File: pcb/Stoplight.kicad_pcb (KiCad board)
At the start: 2 copper layers, 39.7 x 33.1 mm, 13 parts, among them IC1 ATtiny85-20M, IC2 AP7375-33SA-7

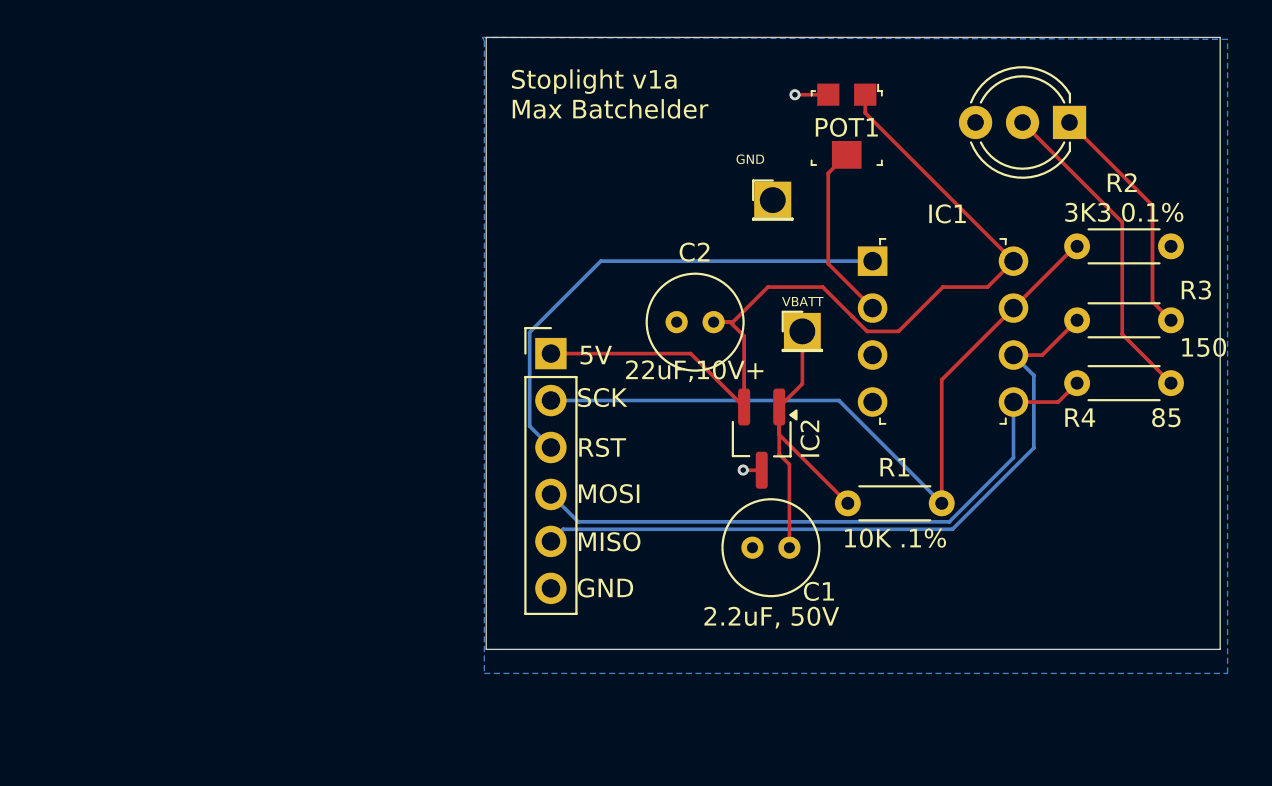
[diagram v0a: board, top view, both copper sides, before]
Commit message: redesigning pcb to be smaller & use tag-connect
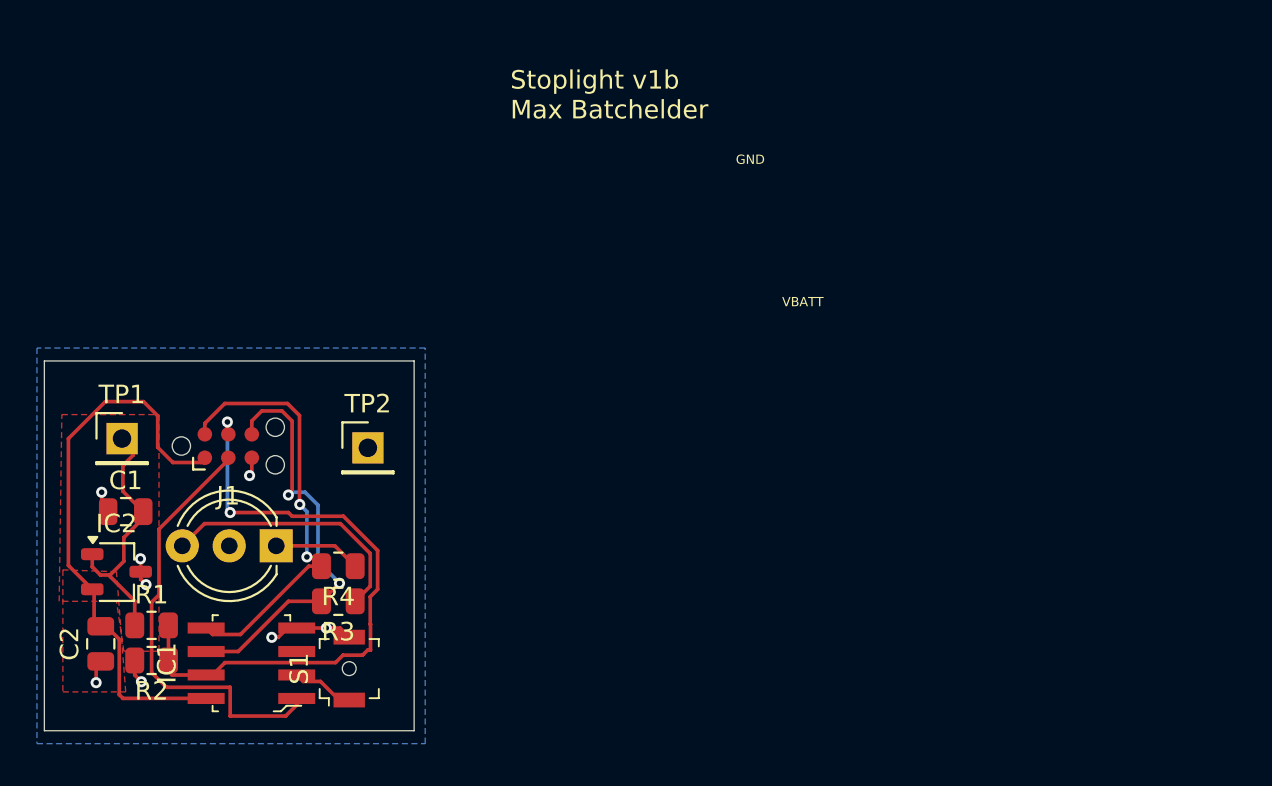
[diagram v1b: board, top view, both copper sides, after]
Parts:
- removed POT1: TC33X-2-103E, digikey-footprints:Trimpot_3.8mmx3.6mm_TC33X-2-103E
- removed REF**: PinHeader_1x06_P2.54mm_Vertical, Connector_PinHeader_2.54mm:PinHeader_1x06_P2.54mm_Vertical
- added J1: Conn_ARM_SWD_TagConnect_TC2030-NL, Connector:Tag-Connect_TC2030-IDC-NL_2x03_P1.27mm_Vertical, F.Cu at (110.0, 104.6)
- added S1: B3U-1000P, digikey-footprints:Switch_Tactile_SMD_B3U-1000P, F.Cu at (116.5, 116.6)
- C1, C2: footprint Capacitor_THT:C_Radial_D5.0mm_H5.0mm_P2.00mm -> Capacitor_SMD:C_0805_2012Metric
- IC1: footprint digikey-footprints:DIP-8_W7.62mm -> digikey-footprints:SOIC-8_W3.9mm
- IC2: value AP7375-33SA-7 -> AP7375-50SA-7; footprint Package_TO_SOT_SMD:TSOT-23_HandSoldering -> Package_TO_SOT_SMD:TSOT-23
- R1, R2, R3, R4: footprint Resistor_THT:R_Axial_DIN0204_L3.6mm_D1.6mm_P5.08mm_Horizontal -> Resistor_SMD:R_0805_2012Metric
- TP1, TP2: footprint Connector_PinHeader_2.00mm:PinHeader_1x01_P2.00mm_Vertical -> Connector_PinHeader_2.54mm:PinHeader_1x01_P2.54mm_Vertical
- moved R2 54.8 mm to (105.8, 116.2), turned to 180 degrees
- moved D1 50.9 mm to (110.0, 110.0)
- moved R3 47.5 mm to (115.9, 113.0)
- moved R4 46.1 mm to (115.9, 111.1)
- moved IC1 40.0 mm to (111.2, 116.3), turned to 90 degrees
- moved R1 38.2 mm to (105.8, 114.3)
- moved TP1 37.3 mm to (104.2, 104.2)
- moved C2 35.7 mm to (103.0, 115.3), turned to 90 degrees
- moved IC2 35.6 mm to (103.9, 111.4), turned to 0 degrees
- moved C1 34.0 mm to (104.4, 108.2)
- moved TP2 25.7 mm to (117.5, 104.7)
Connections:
- D1 pad 1: Net-(D1-A1) -> R
- D1 pad 2: Net-(D1-A2) -> GND
- D1 pad 3: GND -> G
- R3 pad 1: Net-(D1-A1) -> G
- R4 pad 1: Net-(D1-A2) -> R
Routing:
- net +5V: track 49.3 -> 30.9 mm
- net Net-(D1-A2): track 17.4 -> 0.00 mm
- net MISO/G: track 37.9 -> 22.8 mm, vias 0 -> 2
- net G: track 0.00 -> 14.3 mm
- net Net-(D1-A1): track 13.0 -> 0.00 mm
- net MOSI/R: track 33.9 -> 23.1 mm, vias 0 -> 2
- net GND: track 2.80 -> 11.0 mm, vias 2 -> 8
- net DIM: track 9.70 -> 2.51 mm
- net SCK/BATT: track 40.4 -> 34.1 mm, vias 0 -> 2
- net +VBATT: track 19.2 -> 14.2 mm
- net R: track 0.00 -> 4.73 mm
- net RST: track 26.9 -> 23.7 mm
- added copper zone on F.Cu, net +5V
- added copper zone on F.Cu, net +VBATT
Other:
- board size 39.7 x 33.1 mm -> 20 x 20 mm
- board text added: "Stoplight v1b Max Batchelder"
- board text removed: "5V"
- board text removed: "MISO"
- board text removed: "MOSI"
- board text removed: "RST"
- board text removed: "SCK"
- board text removed: "Stoplight v1a Max Batchelder"

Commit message: pcb v1b, ready to manufacture
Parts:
- J1: moved to B.Cu
- TP1: footprint Connector_PinHeader_2.54mm:PinHeader_1x01_P2.54mm_Vertical -> TestPoint:TestPoint_Pad_2.0x2.0mm
- TP2: footprint Connector_PinHeader_2.54mm:PinHeader_1x01_P2.54mm_Vertical -> TestPoint:TestPoint_Pad_2.0x2.0mm; moved to B.Cu
- moved TP2 13.3 mm to (104.2, 105.3)
- moved J1 8.74 mm to (115.8, 111.1), turned to 90 degrees
- moved R4 1.16 mm to (115.4, 110.0)
- moved TP1 1.15 mm to (104.2, 105.3)
- moved D1 1.01 mm to (110.2, 111.0)
- moved R3 0.90 mm to (116.1, 112.1)
- moved S1 0.24 mm to (116.7, 116.6)
- moved IC2 0.23 mm to (104.1, 111.4)
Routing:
- net SCK/BATT: track 34.1 -> 17.9 mm, vias 2 -> 1
- net +5V: track 30.9 -> 23.6 mm, vias 0 -> 1
- net MOSI/R: track 23.1 -> 20.0 mm, vias 2 -> 1
- net GND: track 11.0 -> 8.00 mm, vias 8 -> 7
- net R: track 4.73 -> 6.93 mm
- net G: track 14.3 -> 16.1 mm
- net MISO/G: track 22.8 -> 24.4 mm, vias 2 -> 1
- net RST: track 23.7 -> 22.1 mm, vias 0 -> 1
- net DIM: track 2.51 -> 3.88 mm
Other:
- board size 20 x 20 mm -> 17.2 x 16.4 mm

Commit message: v1b PCB as ordered
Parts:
- removed IC1: ATtiny85-20M, digikey-footprints:SOIC-8_W3.9mm
- added U1: ATtiny85-20MU, Package_DFN_QFN:QFN-20-1EP_4x4mm_P0.5mm_EP2.6x2.6mm, F.Cu at (110.6, 115.9)
- C1: footprint Capacitor_SMD:C_0805_2012Metric -> Capacitor_SMD:C_0603_1608Metric
- C2: footprint Capacitor_SMD:C_0805_2012Metric -> Capacitor_SMD:C_0402_1005Metric
- J1, TP2: moved to F.Cu
- R1, R2, R3: footprint Resistor_SMD:R_0805_2012Metric -> Resistor_SMD:R_0402_1005Metric
- R4: value 85 -> 82; footprint Resistor_SMD:R_0805_2012Metric -> Resistor_SMD:R_0402_1005Metric
- moved R3 9.47 mm to (107.0, 114.8), turned to 0 degrees
- moved R4 9.25 mm to (107.0, 114.0), turned to 0 degrees
- moved R2 6.93 mm to (106.2, 109.3), turned to 90 degrees
- moved R1 5.05 mm to (105.3, 109.3), turned to -90 degrees
- moved TP1 2.40 mm to (103.1, 107.5)
- moved C1 1.73 mm to (103.3, 109.5), turned to 180 degrees
- moved TP2 1.32 mm to (103.1, 104.7)
- moved C2 1.01 mm to (102.9, 114.3), turned to 0 degrees
- moved S1 0.95 mm to (116.0, 116.0), turned to 0 degrees
- moved J1 0.63 mm to (116.4, 110.8)
- moved IC2 0.53 mm to (104.1, 112.0)
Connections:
- J1 pad 1: +5V -> MISO/G
- J1 pad 2: MOSI/R -> +5V
- J1 pad 3: RST -> SCK/BATT
- J1 pad 4: SCK/BATT -> MOSI/R
- J1 pad 5: GND -> RST
- J1 pad 6: MISO/G -> GND
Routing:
- net SCK/BATT: track 17.9 -> 30.1 mm, vias 1 -> 2
- net G: track 16.1 -> 5.02 mm
- net GND: track 8.00 -> 18.5 mm, vias 7 -> 12
- net RST: track 22.1 -> 13.0 mm, vias 1 -> 0
- net MOSI/R: track 20.0 -> 11.1 mm, vias 1 -> 0
- net +VBATT: track 14.3 -> 7.35 mm
- net +5V: track 23.6 -> 26.9 mm, vias 1 -> 2
- net DIM: track 3.88 -> 1.88 mm
- net MISO/G: track 24.4 -> 23.0 mm, vias 1 -> 2
- net R: track 6.93 -> 7.63 mm
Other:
- outline, holes or cut-outs redrawn
